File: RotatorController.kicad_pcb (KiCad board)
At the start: 2 copper layers, 100 x 70.9 mm, 59 parts, among them J1 USB_A, J2 26 VAC, J3 Rotator, J4 Motor Cap, K1 G5LE-1, K2 G5LE-1, K3 G5LE-1, Q1 BSS123, Q2 BSS123, Q3 BSS123, SW1 SW_CW, SW2 SW_CCW, U1 Teensy4.0, U3 AP2161W

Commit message: Homing in on final release add ground to pot and button mounting pads added start of dimensions and front panel sketch
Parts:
- removed J3: Rotator, Connector_TE-Connectivity:TE_MATE-N-LOK_1-770970-x_2x04_P4.14mm_Horizontal
- C11: moved to B.Cu
- D13, D19, D5, D7: footprint LED_SMD:LED_miniPLCC_2315_Handsoldering -> LED_SMD:LED_0805_2012Metric_Pad1.15x1.40mm_HandSolder
- J2: value 26 VAC -> Rotator; footprint Connector_TE-Connectivity:TE_MATE-N-LOK_1-770966-x_1x02_P4.14mm_Horizontal -> Connector_TE-Connectivity:TE_MATE-N-LOK_1-770971-x_2x05_P4.14mm_Horizontal
- RV1: value R_Potentiometer_US -> Az_Preset
- SW1: value SW_CW -> CW
- SW2: value SW_CCW -> CCW
- moved J1 94.9 mm to (186.7, 91.7), turned to 90 degrees
- moved D1 75.9 mm to (175.8, 88.0), turned to 0 degrees
- moved D4 73.2 mm to (113.2, 58.5), turned to 0 degrees
- moved D2 71.5 mm to (175.8, 93.0), turned to 0 degrees
- moved U3 68.6 mm to (175.6, 98.0), turned to 180 degrees
- moved R1 63.7 mm to (118.2, 58.5), turned to 0 degrees
- moved D17 42.9 mm to (140.8, 69.0), turned to 90 degrees
- moved C12 34.3 mm to (185.0, 65.5)
- moved C11 32.8 mm to (185.2, 72.5), turned to 180 degrees
- moved R2 24.5 mm to (124.0, 83.2)
- moved D18 22.7 mm to (152.8, 69.0), turned to 90 degrees
- moved D16 22.0 mm to (158.2, 69.0), turned to 90 degrees
- moved D15 20.5 mm to (162.5, 90.0), turned to 0 degrees
- moved R15 20.4 mm to (102.5, 61.0)
- moved C1 18.9 mm to (185.2, 60.8)
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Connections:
- J2 pad 1: GND -> /26VAC
- J2 pad 2: /26VAC -> /Brake
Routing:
- net Net-(D4-K): track 104.0 -> 10.9 mm, vias 0 -> 2
- net /Ctlr_Rx: track 96.8 -> 21.1 mm
- net /Ctlr_Tx: track 98.2 -> 32.6 mm
- net /3V3: track 140.5 -> 189.1 mm
- net Net-(D7-K): track 4.50 -> 28.6 mm
- net /+5V: track 204.9 -> 182.3 mm, vias 6 -> 3
- net /Right: track 63.8 -> 41.2 mm
- net /Wiper+: track 48.6 -> 68.2 mm, vias 2 -> 4
- net /Brake: track 39.7 -> 23.1 mm, vias 1 -> 0
- net Net-(D6-A): track 30.4 -> 14.2 mm
- net /CCW: track 105.1 -> 90.7 mm, vias 4 -> 2
- net /Left: track 47.6 -> 34.0 mm
- net /Cap1: track 9.52 -> 22.3 mm
- net /Wiper-: track 75.5 -> 86.4 mm, vias 2 -> 3
- net /Cap2: track 10.8 -> 20.2 mm
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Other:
- board size 100 x 70.9 mm -> 99 x 70 mm

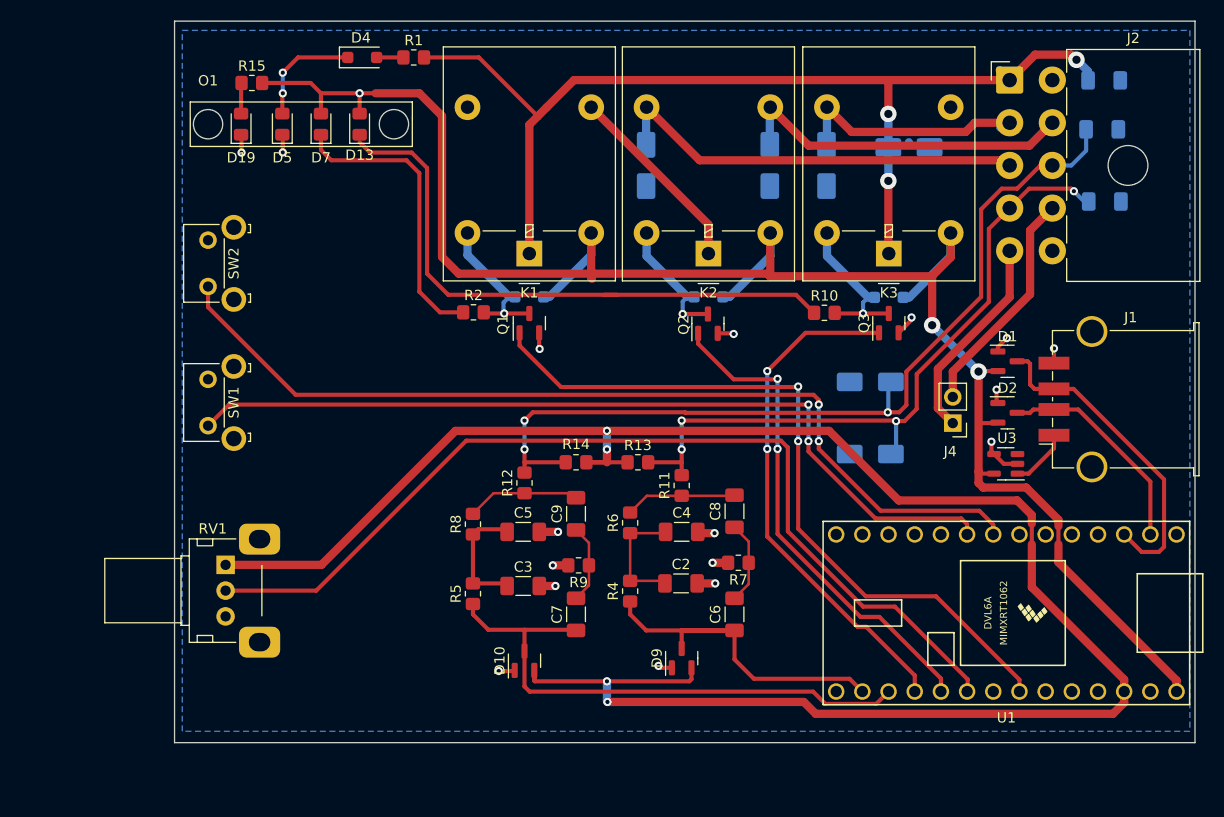
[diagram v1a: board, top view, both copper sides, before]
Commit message: dimensioned drawings of front and back panels corrected switch and pot parts moved connectors and switches to flush with end of board
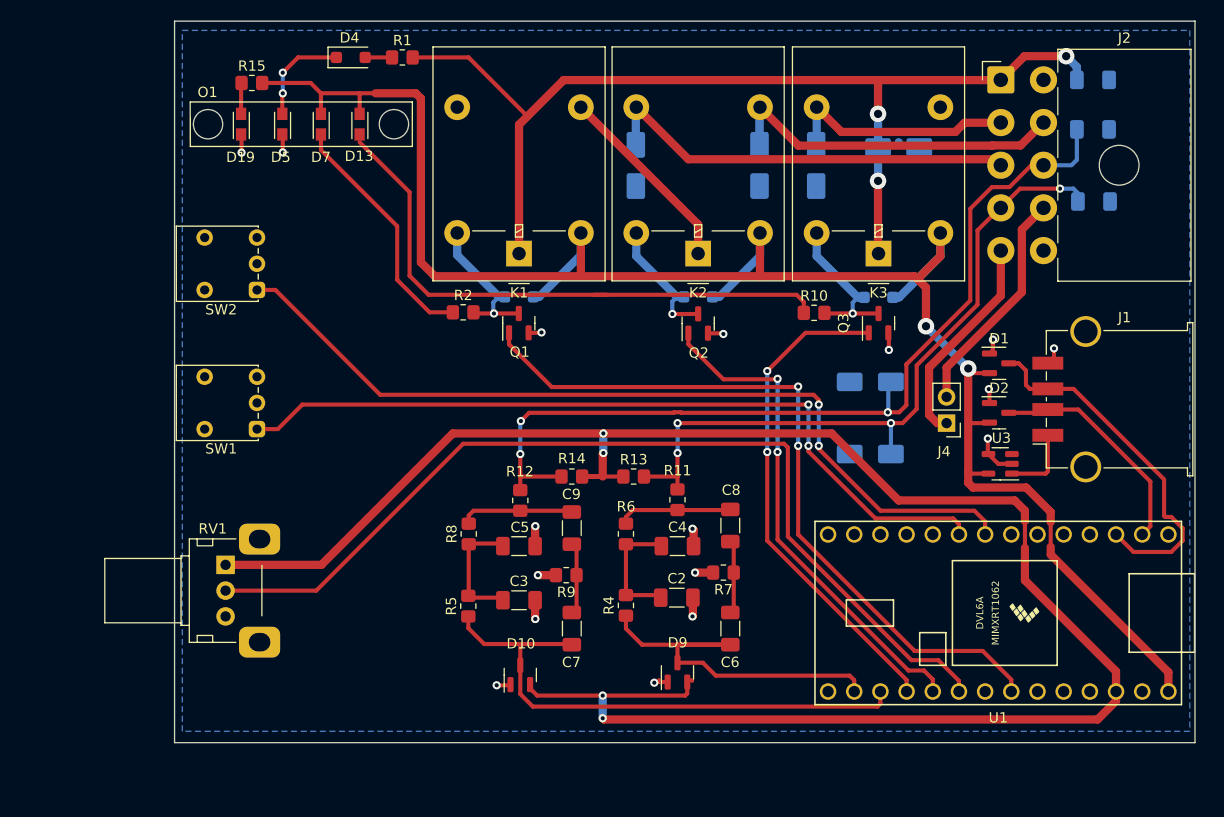
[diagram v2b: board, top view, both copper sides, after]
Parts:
- D13, D19, D7: footprint LED_SMD:LED_0805_2012Metric_Pad1.15x1.40mm_HandSolder -> LED_SMD:LED_miniPLCC_2315_Handsoldering
- D5: value 26VAC -> 26V; footprint LED_SMD:LED_0805_2012Metric_Pad1.15x1.40mm_HandSolder -> LED_SMD:LED_miniPLCC_2315_Handsoldering
- R1: value 560 -> 1000
- SW1, SW2: footprint Button_Switch_THT:SW_SPST_Omron_B3F-315x_Angled -> Button_Switch_THT:SW_Push_1P2T_Vertical_E-Switch_800UDP8P1A1M6
- moved SW1 4.76 mm to (103.0, 94.6), turned to 180 degrees
- moved SW2 4.76 mm to (103.0, 81.1), turned to 180 degrees
- moved R12 1.75 mm to (128.5, 101.5)
- moved R7 1.73 mm to (148.2, 108.5)
- moved R9 1.53 mm to (133.0, 108.8)
- moved C2 1.44 mm to (143.7, 110.9)
- moved C3 1.44 mm to (128.4, 111.2)
- moved C4 1.44 mm to (143.8, 105.9)
- moved C5 1.44 mm to (128.4, 105.9)
- moved C6 1.44 mm to (148.9, 113.9)
- moved C7 1.44 mm to (133.5, 113.9)
- moved C8 1.44 mm to (148.9, 103.9)
- moved C9 1.44 mm to (133.5, 104.2)
- moved D10 1.44 mm to (128.5, 118.4)
- moved D9 1.44 mm to (143.8, 118.2)
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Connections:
- net /Hdg renamed /AzPre
- RV1 pad MP: (no net) -> GND
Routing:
- net /CCW: track 90.7 -> 84.0 mm
- net /CW: track 83.0 -> 77.3 mm
- net Net-(D7-K): track 28.6 -> 23.9 mm
- net /Ctlr_Tx: track 32.6 -> 35.7 mm
- net /Flt_W+: track 35.8 -> 38.2 mm
- net /Wiper-: track 86.4 -> 88.8 mm
- net /Brk_Ctl: track 49.9 -> 48.1 mm
- net Net-(D13-K): track 58.2 -> 56.6 mm
- net /26VAC: track 102.8 -> 101.5 mm
- net Net-(J1-VBUS): track 5.82 -> 7.07 mm
- net /Ctlr_Rx: track 21.1 -> 22.2 mm
- net Net-(D4-K): track 10.9 -> 9.82 mm
- net /+5V: track 182.3 -> 183.4 mm, vias 3 -> 2
- net /AzPre: track 93.6 -> 92.7 mm
- net Net-(C6-Pad2): track 8.01 -> 7.15 mm
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
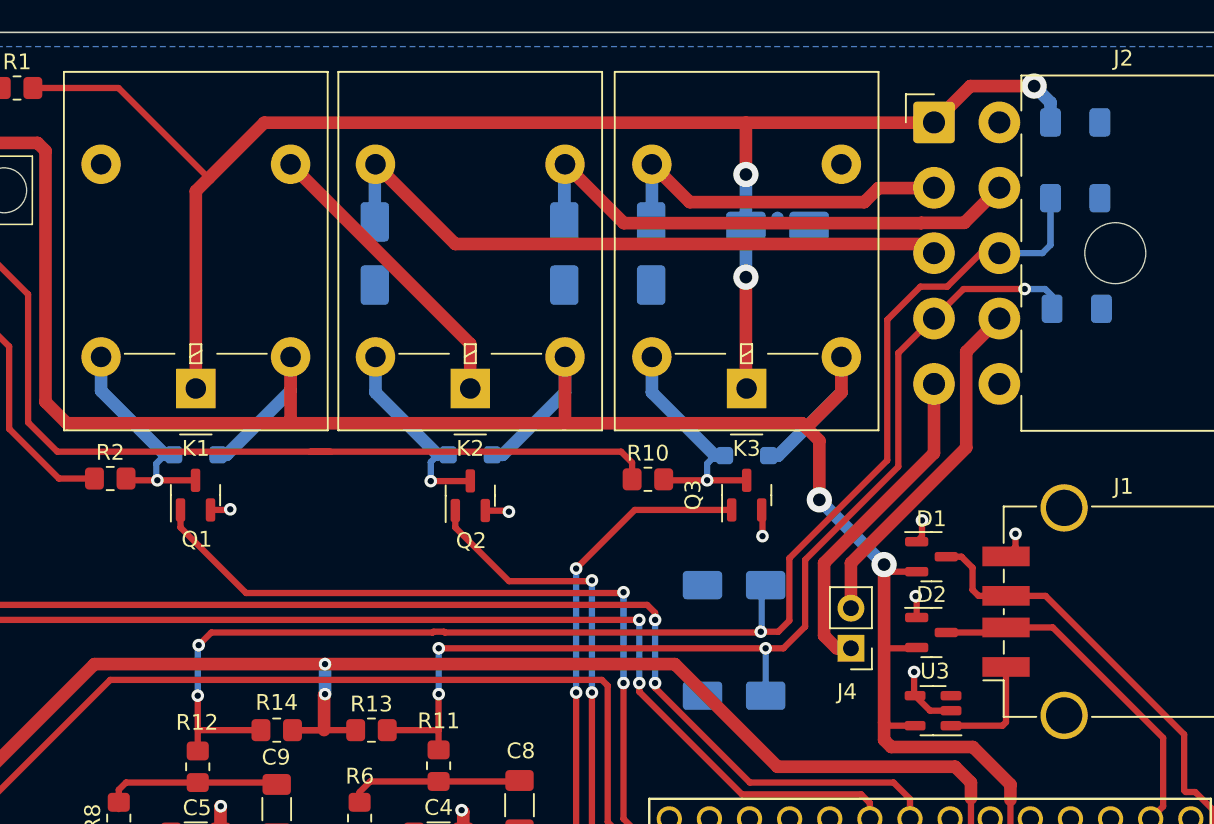
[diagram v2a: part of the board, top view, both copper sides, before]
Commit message: fine tuned layout to shorten bypass cap ground and to reduce ground plane breaks
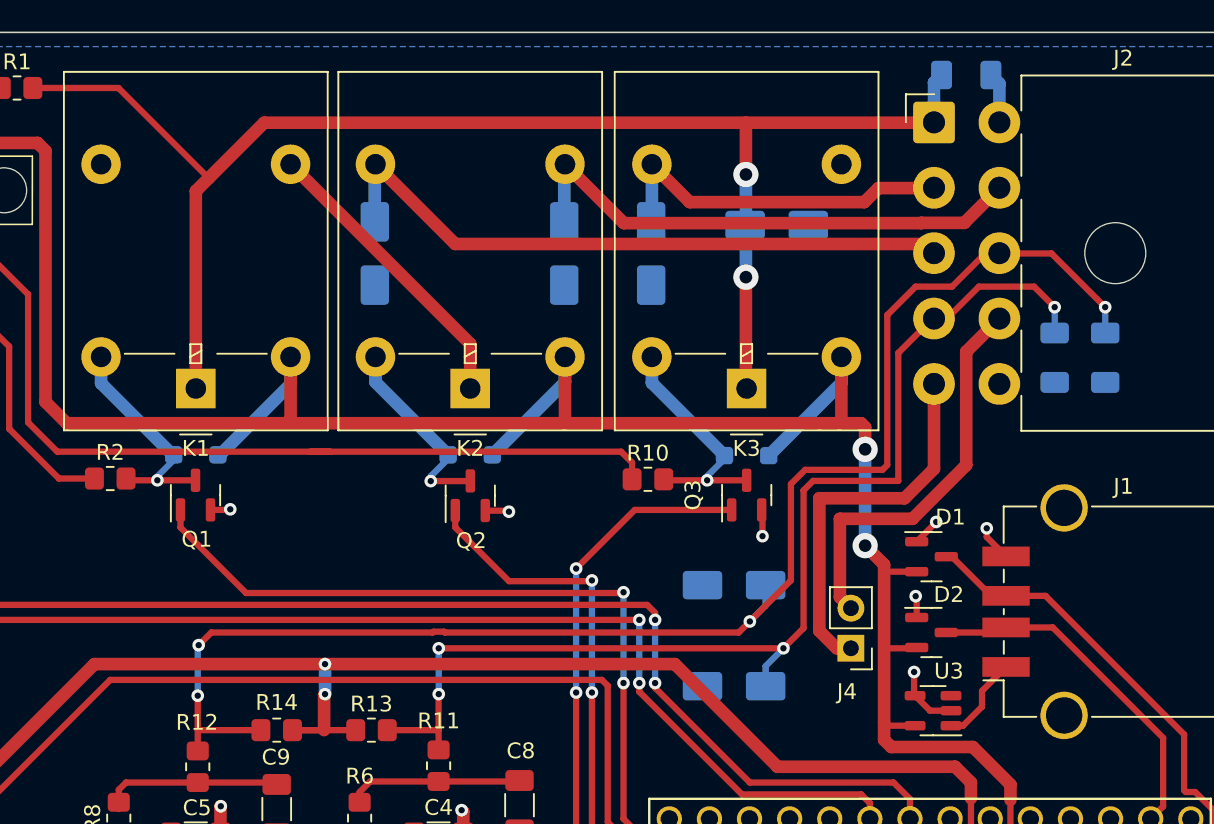
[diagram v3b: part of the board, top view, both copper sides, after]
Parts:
- moved C12 10.3 mm to (186.0, 75.6), turned to 90 degrees
- moved C1 7.52 mm to (177.2, 57.7)
- moved C11 3.40 mm to (182.8, 75.6), turned to 90 degrees
- moved D14 0.60 mm to (162.5, 96.4)
- moved D3 0.07 mm to (165.2, 67.2)
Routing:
- net /26VAC: track 101.5 -> 94.7 mm, vias 3 -> 2
- net /Wiper-: track 88.8 -> 93.4 mm, vias 3 -> 4
- net /Wiper+: track 68.8 -> 73.3 mm
- net GND: track 31.0 -> 34.8 mm
- net /Cap2: track 20.9 -> 24.3 mm
- net /Cap1: track 22.2 -> 25.5 mm
- net Net-(J1-VBUS): track 7.07 -> 5.61 mm
- net /Ctlr_Tx: track 35.7 -> 34.9 mm
- net /+5V: track 183.4 -> 182.9 mm
- net Net-(D8-A): track 12.1 -> 12.7 mm

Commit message: finish cleanup of deleted and renamed datasheets, stage and commits trivial changes to pcb and sch
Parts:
- removed D1, D2: BAS40-04, Package_TO_SOT_SMD:SOT-23
- removed D19: 5V, LED_SMD:LED_miniPLCC_2315_Handsoldering
- removed J1: USB_A, Connector_USB:USB_A_TE_292303-7_Horizontal
- removed J4: Motor Cap, Connector_PinHeader_2.54mm:PinHeader_1x02_P2.54mm_Vertical
- removed R15: 560, Resistor_SMD:R_0805_2012Metric_Pad1.20x1.40mm_HandSolder
- removed U3: AP2161W, Package_TO_SOT_SMD:SOT-23-5
- added J3: Controller, Connector_TE-Connectivity:TE_MATE-N-LOK_1-770970-x_2x04_P4.14mm_Horizontal, F.Cu at (175.2, 83.8)
- D5: value 26V -> 26VAC
- SW1: footprint Button_Switch_THT:SW_Push_1P2T_Vertical_E-Switch_800UDP8P1A1M6 -> Button_Switch_THT:SW_SPST_Omron_B3F-315x_Angled
- SW2: value CCW -> CW; footprint Button_Switch_THT:SW_Push_1P2T_Vertical_E-Switch_800UDP8P1A1M6 -> Button_Switch_THT:SW_SPST_Omron_B3F-315x_Angled
- moved C1 6.25 mm to (183.2, 59.2), turned to -90 degrees
- moved SW1 5.53 mm to (97.5, 94.0), turned to 90 degrees
- moved SW2 5.50 mm to (97.5, 81.0), turned to 90 degrees
- moved J2 1.21 mm to (175.3, 59.5)
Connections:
- RV1 pad MP: GND -> (no net)
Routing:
- net /Ctlr_Tx: track 34.9 -> 0.00 mm
- net /Ctlr_Rx: track 22.2 -> 0.00 mm
- net /Cap2: track 24.3 -> 7.71 mm
- net GND: track 34.8 -> 21.4 mm, vias 17 -> 13
- net /Cap1: track 25.5 -> 13.6 mm
- net /26VAC: track 94.7 -> 102.7 mm
- net /CCW: track 84.0 -> 90.5 mm
- net /+5V: track 182.9 -> 176.9 mm
- net Net-(J1-VBUS): track 5.61 -> 0.00 mm
- net /CW: track 77.3 -> 82.8 mm
- net Net-(D19-A): track 3.02 -> 0.00 mm
- net (no net): track 0.00 -> 3.02 mm
- net /Wiper+: track 73.3 -> 75.5 mm
- net /Wiper-: track 93.4 -> 95.3 mm
- net /Left: track 33.6 -> 34.3 mm
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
